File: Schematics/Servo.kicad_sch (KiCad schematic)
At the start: 12 parts, among them CN1 Limit Switch Connector 1, CN2 Limit Switch Connector 2, CN3 XY-B3B-XH-A, CN4 XY-B3B-XH-A, U6 TPS22917DBVR

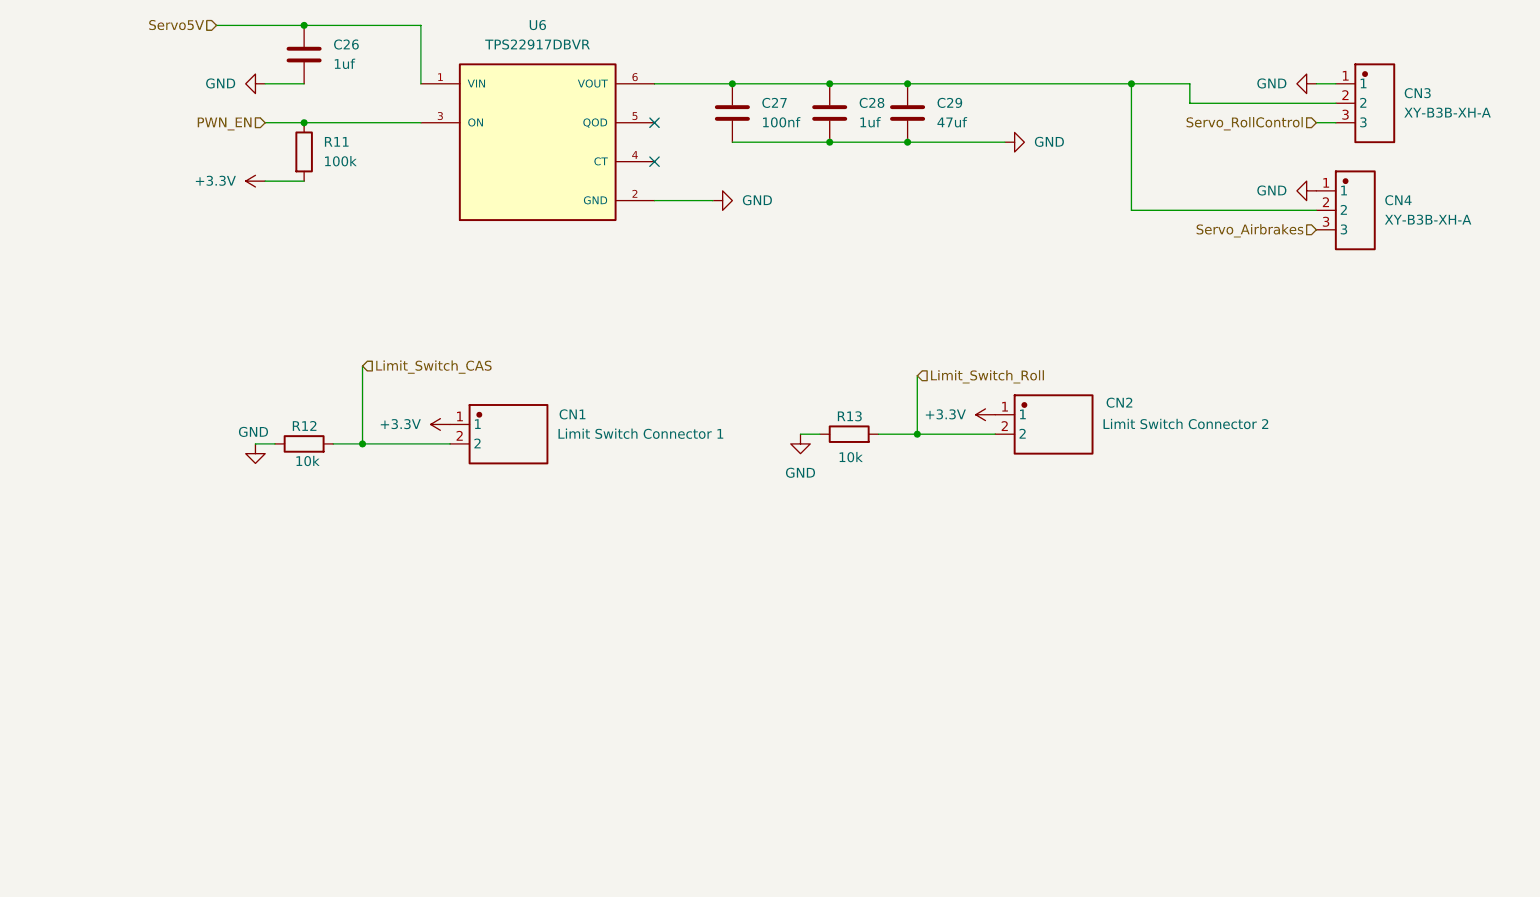
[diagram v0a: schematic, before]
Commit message: started new design with esp32
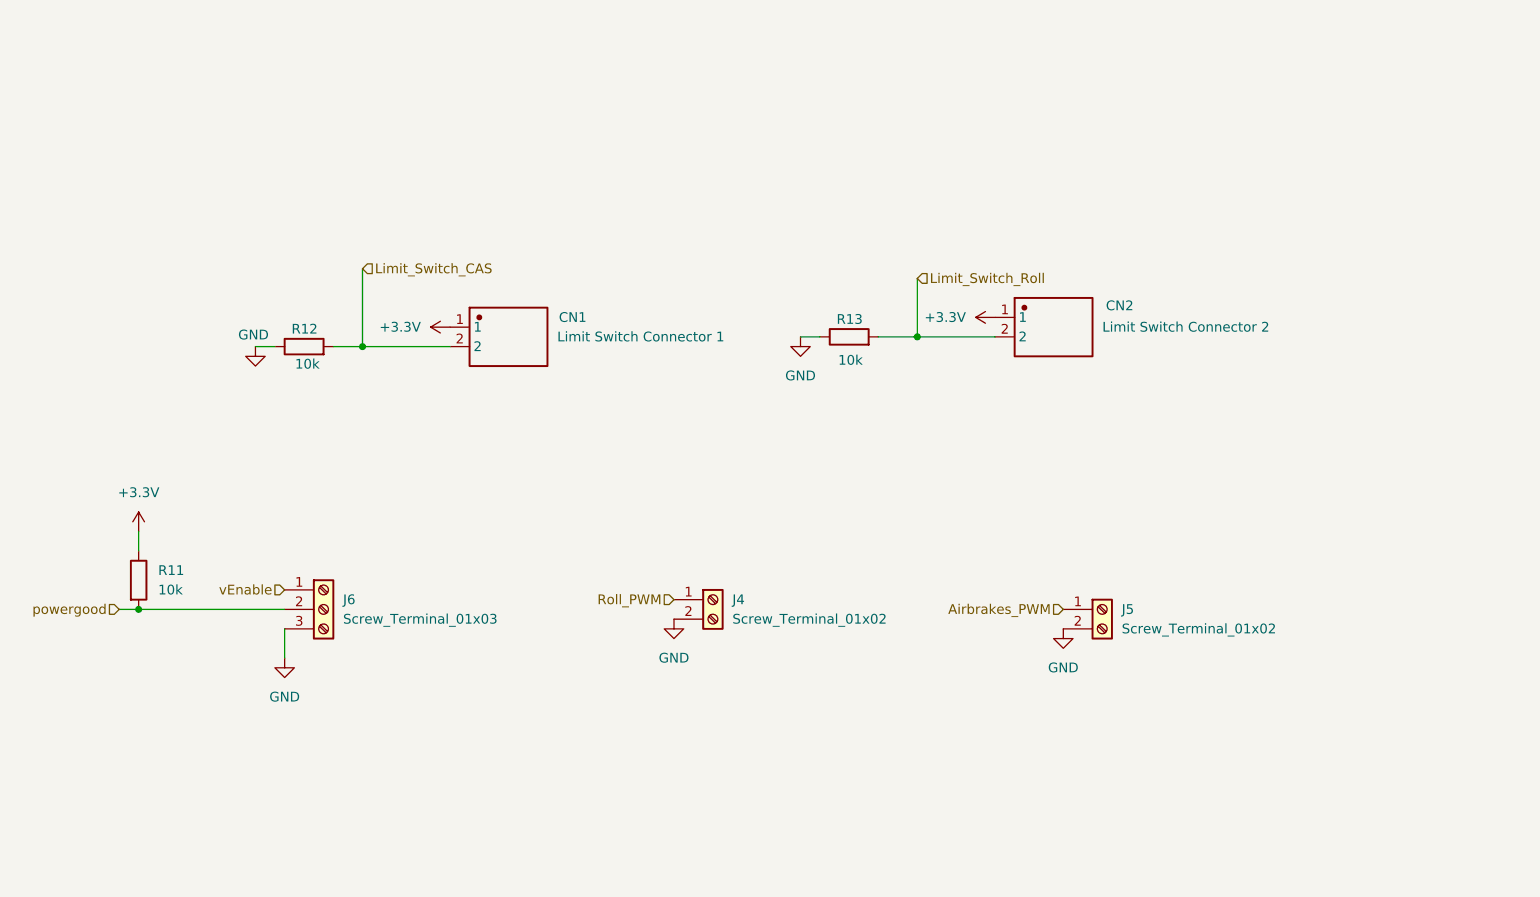
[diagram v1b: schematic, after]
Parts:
- removed C26, C28: 1uf, Capacitor_SMD:C_0805_2012Metric_Pad1.18x1.45mm_HandSolder, symbol Device:C
- removed C27: 100nf, Capacitor_SMD:C_0805_2012Metric_Pad1.18x1.45mm_HandSolder, symbol Device:C
- removed C29: 47uf, Capacitor_SMD:C_0805_2012Metric_Pad1.18x1.45mm_HandSolder, symbol Device:C
- removed CN3, CN4: XY-B3B-XH-A, myFootprints:JST_B3B-XH-A, symbol custom symbols:XY-B3B-XH-A
- removed U6: TPS22917DBVR, myFootprints:SOT95P280X145-6N, symbol TPS22917DBVR:TPS22917DBVR
- added J4, J5: Screw_Terminal_01x02, TerminalBlock_Phoenix:TerminalBlock_Phoenix_PT-1,5-2-3.5-H_1x02_P3.50mm_Horizontal, symbol Connector:Screw_Terminal_01x02
- added J6: Screw_Terminal_01x03, TerminalBlock_Phoenix:TerminalBlock_Phoenix_PT-1,5-3-3.5-H_1x03_P3.50mm_Horizontal, symbol Connector:Screw_Terminal_01x03
- R11: value 100k -> 10k; footprint Resistor_SMD:R_0805_2012Metric_Pad1.20x1.40mm_HandSolder -> (none); LCSC C96346 -> (none)
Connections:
- net PWN_EN is gone; now on net +3.3V: R11.1
- net +3.3V: no longer R11.2
- net GND: now also J4.2 (Pin_2), J5.2 (Pin_2), J6.3 (Pin_3)
- new net Airbrakes_PWM: J5.1 (Pin_1)
- new net Roll_PWM: J4.1 (Pin_1)
- new net powergood: J6.2 (Pin_2), R11.2
- new net vEnable: J6.1 (Pin_1)
- no-connect marks 2 -> 0
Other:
- moved on the sheet: CN1, CN2, R12, R13

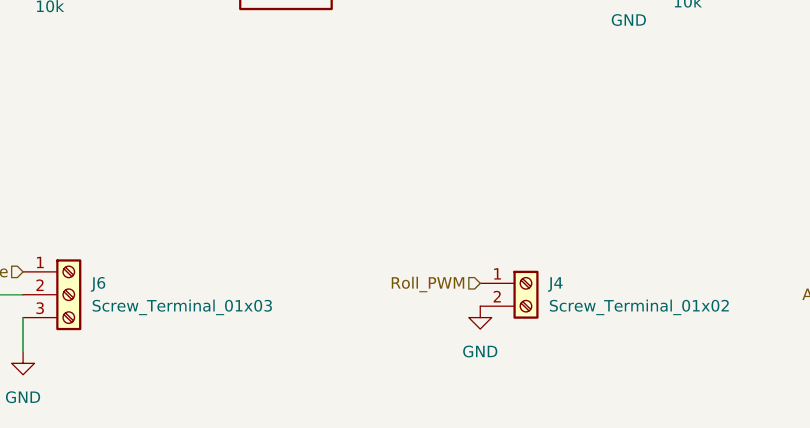
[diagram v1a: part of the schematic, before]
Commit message: finished first layout and routing
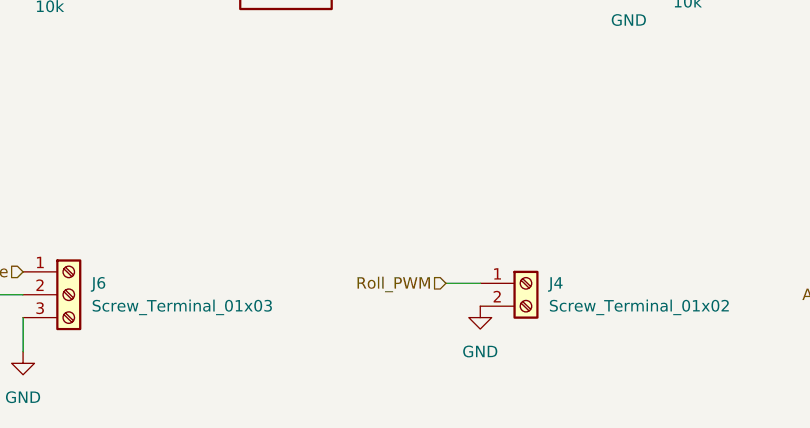
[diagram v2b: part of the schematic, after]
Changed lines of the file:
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@@
+	(wire
+		(pts
+			(xy 125.73 118.11) (xy 129.54 118.11)
+		)
+		(stroke
+			(width 0)
+			(type default)
+		)
+	)
 	(wire
 		(pts
@@
 	(hierarchical_label "Roll_PWM"
 		(shape input)
-		(at 129.54 118.11 180)
+		(at 125.73 118.11 180)
 		(effects
 			(font

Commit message: clean up of routing
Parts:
- J4, J5, J6: LCSC (none) -> C474892
- R11: footprint (none) -> Resistor_SMD:R_0805_2012Metric_Pad1.20x1.40mm_HandSolder; LCSC (none) -> C84376
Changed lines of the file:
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@@
 			)
 		)
-		(property "Footprint" ""
+		(property "Footprint" "Resistor_SMD:R_0805_2012Metric_Pad1.20x1.40mm_HandSolder"
 			(at 57.912 115.57 90)
 			(effects
@@
 		)
 		(property "Description" "Resistor"
+			(at 59.69 115.57 0)
+			(effects
+				(font
+					(size 1.27 1.27)
+				)
+				(hide yes)
+			)
+		)
+		(property "LCSC" "C84376"
 			(at 59.69 115.57 0)
 			(effects
@@
 			)
 		)
+		(property "LCSC" "C474892"
+			(at 83.82 119.38 0)
+			(effects
+				(font
+					(size 1.27 1.27)
+				)
+				(hide yes)
+			)
+		)
 		(pin "2"
 		)
@@
 			)
 		)
+		(property "LCSC" "C474892"
+			(at 134.62 118.11 0)
+			(effects
+				(font
+					(size 1.27 1.27)
+				)
+				(hide yes)
+			)
+		)
 		(pin "2"
 		)
@@
 			(at 185.42 119.38 0)
 			(effects
+				(font
+					(size 1.27 1.27)
+				)
+				(hide yes)
+			)
+		)
+		(property "LCSC" "C474892"
+			(at 185.42 119.38 0)
+			(effects

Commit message: updated board waiting on review
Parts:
- J4, J5: footprint TerminalBlock_Phoenix:TerminalBlock_Phoenix_PT-1,5-2-3.5-H_1x02_P3.50mm_Horizontal -> Connector_JST:JST_XH_B2B-XH-AM_1x02_P2.50mm_Vertical
- J6: footprint TerminalBlock_Phoenix:TerminalBlock_Phoenix_PT-1,5-3-3.5-H_1x03_P3.50mm_Horizontal -> Connector_JST:JST_EH_B3B-EH-A_1x03_P2.50mm_Vertical

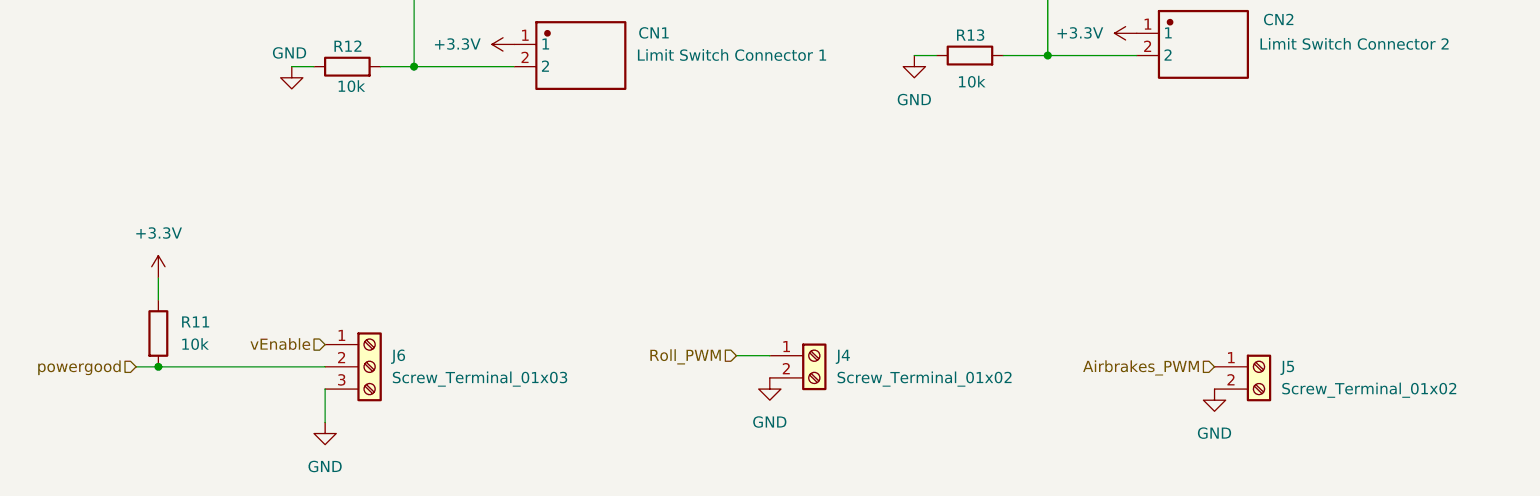
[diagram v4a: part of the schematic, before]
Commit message: removed esp32 to seperate board, added gps breakout, pending final review for purchase
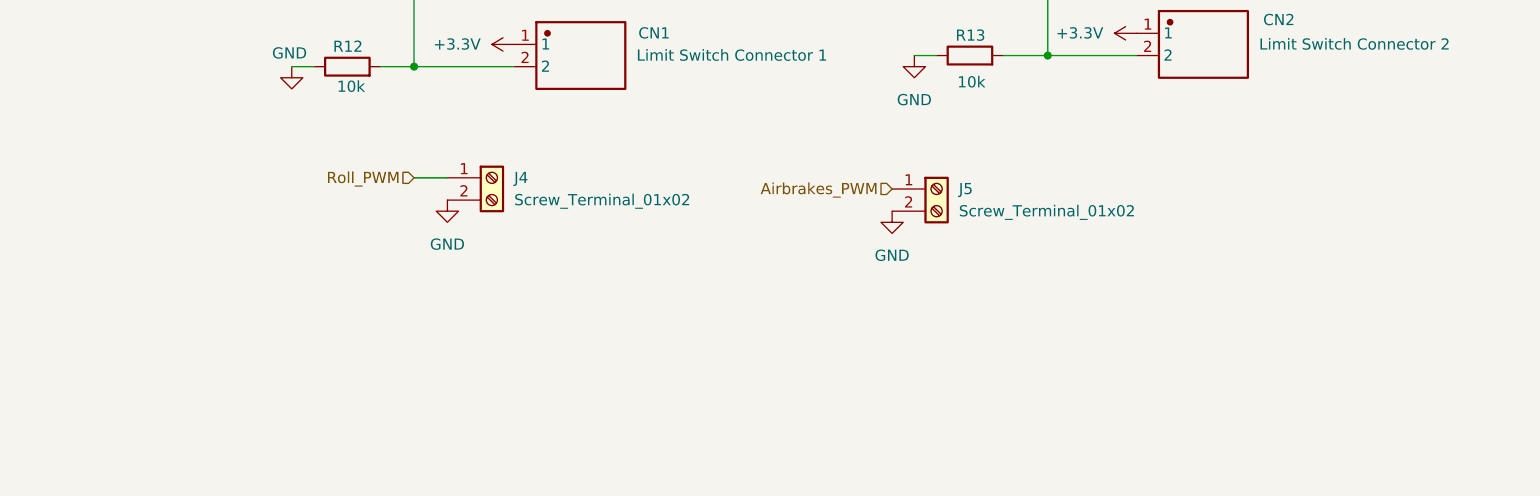
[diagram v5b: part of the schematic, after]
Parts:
- removed J6: Screw_Terminal_01x03, Connector_JST:JST_EH_B3B-EH-A_1x03_P2.50mm_Vertical, symbol Connector:Screw_Terminal_01x03
- removed R11: 10k, Resistor_SMD:R_0805_2012Metric_Pad1.20x1.40mm_HandSolder, symbol Device:R
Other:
- moved on the sheet: J4, J5

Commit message: finished waiting for review
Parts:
- added D3, D6: D_Schottky, Diode_SMD:D_SOD-123, symbol Device:D_Schottky
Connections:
- net Airbrakes_PWM: now also D6.2 (A); no longer J5.1 (Pin_1)
- net Roll_PWM: now also D3.2 (A); no longer J4.1 (Pin_1)
- new net: D6.1 (K), J5.1 (Pin_1)
- new net: D3.1 (K), J4.1 (Pin_1)
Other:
- moved on the sheet: J5
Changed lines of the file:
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@@
+	(wire
+		(pts
+			(xy 74.93 97.79) (xy 66.04 97.79)
+		)
+		(stroke
+			(width 0)
+			(type default)
+		)
+	)
 	(wire
 		(pts
@@
 	(wire
 		(pts
-			(xy 88.9 85.09) (xy 88.9 74.93)
+			(xy 163.83 99.06) (xy 173.99 99.06)
 		)
 		(stroke
@@
 	(wire
 		(pts
-			(xy 74.93 85.09) (xy 77.47 85.09)
+			(xy 88.9 85.09) (xy 88.9 74.93)
 		)
 		(stroke
@@
 	(wire
 		(pts
-			(xy 88.9 97.79) (xy 92.71 97.79)
+			(xy 74.93 85.09) (xy 77.47 85.09)
 		)
 		(stroke
@@
 		)
 	)
+	(wire
+		(pts
+			(xy 82.55 97.79) (xy 92.71 97.79)
+		)
+		(stroke
+			(width 0)
+			(type default)
+		)
+	)
+	(wire
+		(pts
+			(xy 173.99 101.6) (xy 143.51 101.6)
+		)
+		(stroke
+			(width 0)
+			(type default)
+		)
+	)
+	(wire
+		(pts
+			(xy 156.21 99.06) (xy 143.51 99.06)
+		)
+		(stroke
+			(width 0)
+			(type default)
+		)
+	)
 	(hierarchical_label "Roll_PWM"
 		(shape input)
-		(at 88.9 97.79 180)
+		(at 66.04 97.79 180)
 		(effects
 			(font
@@
 	)
 	(symbol
+		(lib_id "Device:D_Schottky")
+		(at 160.02 99.06 180)
+		(unit 1)
+		(body_style 1)
+		(exclude_from_sim no)
+		(in_bom yes)
+		(on_board yes)
+		(in_pos_files yes)
+		(dnp no)
+		(fields_autoplaced yes)
+		(property "Reference" "D6"
+			(at 160.3375 92.71 0)
+			(show_name no)
+			(do_not_autoplace no)
+			(effects
+				(font
+					(size 1.27 1.27)
+				)
+			)
+		)
+		(property "Value" "D_Schottky"
+			(at 160.3375 95.25 0)
+			(show_name no)
+			(do_not_autoplace no)
+			(effects
+				(font
+					(size 1.27 1.27)
+				)
+			)
+		)
+		(property "Footprint" "Diode_SMD:D_SOD-123"
+			(at 160.02 99.06 0)
+			(hide yes)
+			(show_name no)
+			(do_not_autoplace no)
+			(effects
+				(font
+					(size 1.27 1.27)
+				)
+			)
+		)
+		(property "Datasheet" ""
+			(at 160.02 99.06 0)
+			(hide yes)
+			(show_name no)
+			(do_not_autoplace no)
+			(effects
+				(font
+					(size 1.27 1.27)
+				)
+			)
+		)
+		(property "Description" "Schottky diode"
+			(at 160.02 99.06 0)
+			(hide yes)
+			(show_name no)
+			(do_not_autoplace no)
+			(effects
+				(font
+					(size 1.27 1.27)
+				)
+			)
+		)
+		(pin "1"
+		)
+		(pin "2"
+		)
+		(instances
+			(project "CAN-Interface-Board"
+				(path "/8a3e7f99-4046-40e8-bd7c-d9d1c8c7162e/992c9dbe-cf65-4f66-b0f4-1615492bebdc"
+					(reference "D6")
+					(unit 1)
+				)
+			)
+		)
+	)
+	(symbol
 		(lib_id "custom symbols:JST B2B-XH-A(LF)(SN)")
 		(at 106.68 83.82 0)
@@
 	)
 	(symbol
+		(lib_id "Device:D_Schottky")
+		(at 78.74 97.79 180)
+		(unit 1)
+		(body_style 1)
+		(exclude_from_sim no)
+		(in_bom yes)
+		(on_board yes)
+		(in_pos_files yes)
+		(dnp no)
+		(fields_autoplaced yes)
+		(property "Reference" "D3"
+			(at 79.0575 91.44 0)
+			(show_name no)
+			(do_not_autoplace no)
+			(effects
+				(font
+					(size 1.27 1.27)
+				)
+			)
+		)
+		(property "Value" "D_Schottky"
+			(at 79.0575 93.98 0)
+			(show_name no)
+			(do_not_autoplace no)
+			(effects
+				(font
+					(size 1.27 1.27)
+				)
+			)
+		)
+		(property "Footprint" "Diode_SMD:D_SOD-123"
+			(at 78.74 97.79 0)
+			(hide yes)
+			(show_name no)
+			(do_not_autoplace no)
+			(effects
+				(font
+					(size 1.27 1.27)
+				)
+			)
+		)
+		(property "Datasheet" ""
+			(at 78.74 97.79 0)
+			(hide yes)
+			(show_name no)
+			(do_not_autoplace no)
+			(effects
+				(font
+					(size 1.27 1.27)
+				)
+			)
+		)
+		(property "Description" "Schottky diode"
+			(at 78.74 97.79 0)
+			(hide yes)
+			(show_name no)
+			(do_not_autoplace no)
+			(effects
+				(font
+					(size 1.27 1.27)
+				)
+			)
+		)
+		(pin "1"
+		)
+		(pin "2"
+		)
+		(instances
+			(project "CAN-Interface-Board"
+				(path "/8a3e7f99-4046-40e8-bd7c-d9d1c8c7162e/992c9dbe-cf65-4f66-b0f4-1615492bebdc"
+					(reference "D3")
+					(unit 1)
+				)
+			)
+		)
+	)
+	(symbol
 		(lib_id "power:+3.3V")
 		(at 100.33 82.55 90)
@@
 	(symbol
 		(lib_id "Connector:Screw_Terminal_01x02")
-		(at 148.59 99.06 0)
+		(at 179.07 99.06 0)
 		(unit 1)
 		(body_style 1)
@@
 		(fields_autoplaced yes)
 		(property "Reference" "J5"
-			(at 151.13 99.0599 0)
+			(at 181.61 99.0599 0)
 			(show_name no)
 			(do_not_autoplace no)
@@
 		)
 		(property "Value" "Screw_Terminal_01x02"
-			(at 151.13 101.5999 0)
+			(at 181.61 101.5999 0)
 			(show_name no)
 			(do_not_autoplace no)
@@
 		)
 		(property "Footprint" "Connector_JST:JST_XH_B2B-XH-AM_1x02_P2.50mm_Vertical"
-			(at 148.59 99.06 0)
+			(at 179.07 99.06 0)
 			(hide yes)
 			(show_name no)
@@
 		)
 		(property "Datasheet" ""
-			(at 148.59 99.06 0)
+			(at 179.07 99.06 0)
 			(hide yes)
 			(show_name no)
@@
 		)
 		(property "Description" "Generic screw terminal, single row, 01x02, script generated (kicad-library-utils/schlib/autogen/connector/)"
-			(at 148.59 99.06 0)
+			(at 179.07 99.06 0)
 			(hide yes)
 			(show_name no)
@@
 		)
 		(property "LCSC" "C474892"
-			(at 148.59 99.06 0)
-			(hide yes)
-			(show_name no)
+			(at 179.07 99.06 0)
+			(hide yes)
+			(show_name no)

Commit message: final draft, in JLPCB cart
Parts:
- removed D3, D6: D_Schottky, Diode_SMD:D_SOD-123, symbol Device:D_Schottky
- CN1, CN2: footprint myFootprints:JST_B2B-XH-A_LF__SN_ -> Connector_JST:JST_EH_B2B-EH-A_1x02_P2.50mm_Vertical
- J4, J5: footprint Connector_JST:JST_XH_B2B-XH-AM_1x02_P2.50mm_Vertical -> Connector_JST:JST_EH_B2B-EH-A_1x02_P2.50mm_Vertical; symbol Connector:Screw_Terminal_01x02 -> Connector:Conn_01x02_Pin; LCSC C474892 -> C158012
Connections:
- net +3.3V: now also CN1.2, CN2.2; no longer CN1.1, CN2.1
- net Airbrakes_PWM: now also J5.2 (Pin_2)
- net GND: now also J4.1 (Pin_1), J5.1 (Pin_1); no longer J4.2 (Pin_2), J5.2 (Pin_2)
- net Limit_Switch_CAS: now also CN1.1; no longer CN1.2
- net Limit_Switch_Roll: now also CN2.1; no longer CN2.2
- net Roll_PWM: now also J4.2 (Pin_2)
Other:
- moved on the sheet: CN1, CN2, R12, R13
